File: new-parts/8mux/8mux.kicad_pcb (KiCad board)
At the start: 2 copper layers, 68.6 x 73.7 mm, 9 parts, among them J1 BHR-10-VUA, J2 BHR-10-VUA, J3 BHR-10-VUA, J4 Conn_01x01, K1 J104D2C12VDC.15S, K2 J104D2C12VDC.15S, K3 J104D2C12VDC.15S, K4 J104D2C12VDC.15S

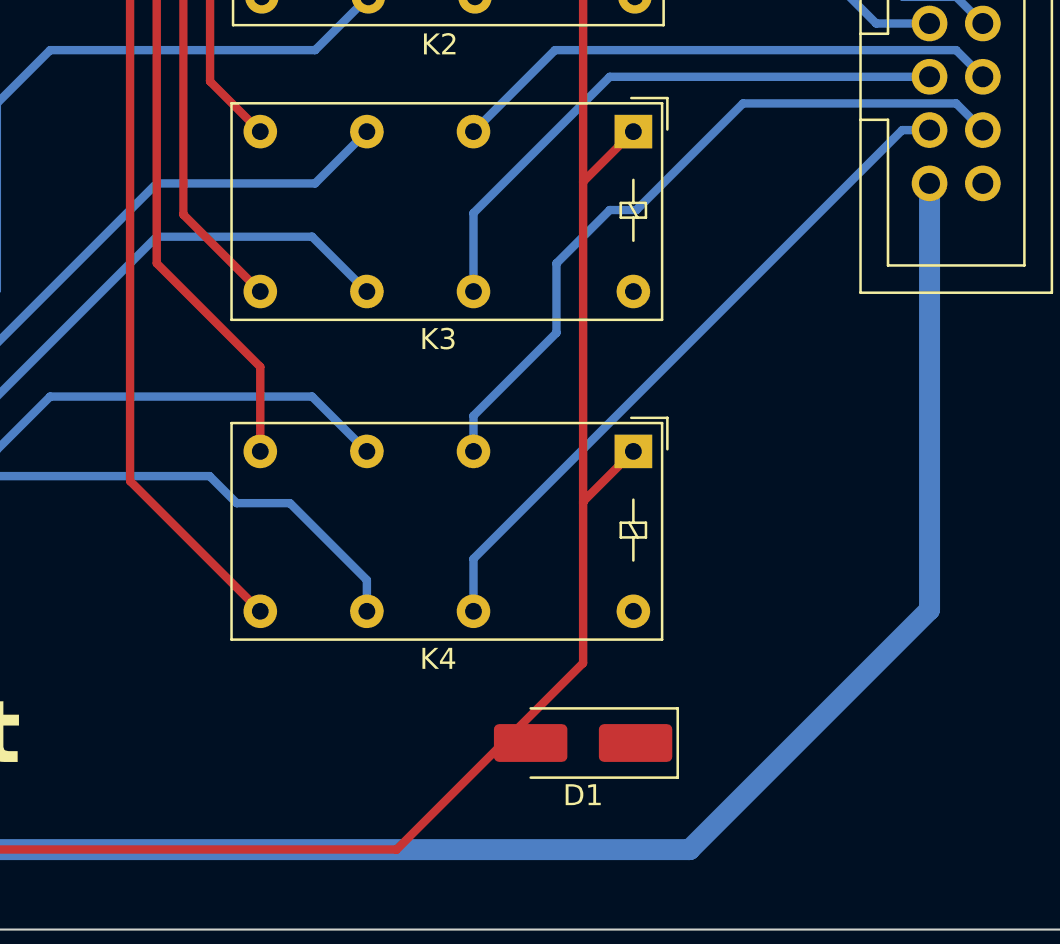
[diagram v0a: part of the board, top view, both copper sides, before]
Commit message: 8mux: Even out relay placement.
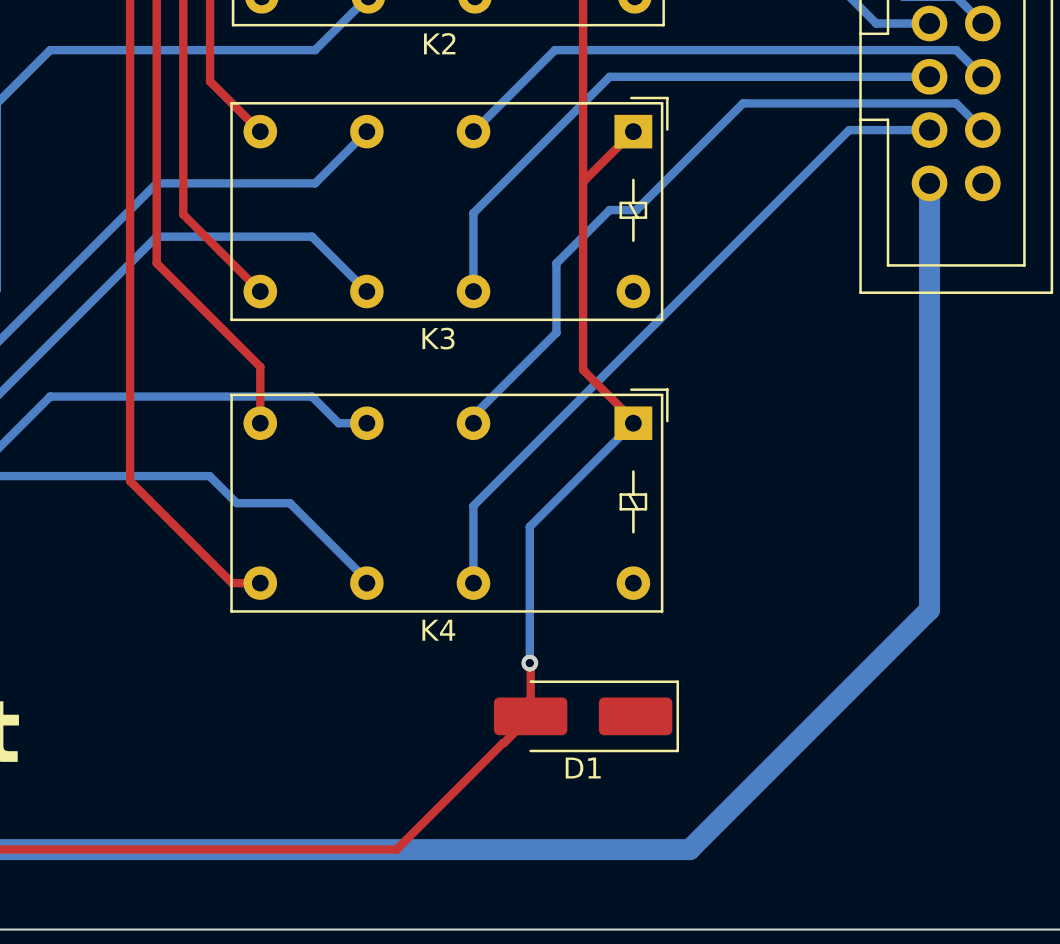
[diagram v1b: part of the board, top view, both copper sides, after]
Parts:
- moved K4 1.34 mm to (151.0, 113.0)
- moved D1 1.27 mm to (148.6, 127.0)
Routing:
- net Net-(D1-A2): track 106.5 -> 103.8 mm, vias 0 -> 1
- net Net-(J3-Pin_8): track 34.6 -> 33.3 mm
- net Net-(J2-Pin_7): track 30.6 -> 29.2 mm
- net Net-(J1-Pin_8): track 45.1 -> 43.7 mm
- net Net-(J2-Pin_8): track 26.1 -> 25.6 mm
- net Net-(J1-Pin_7): track 53.8 -> 53.2 mm
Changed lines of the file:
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@@
   )
   (footprint "Diode_SMD:D_SMA_Handsoldering" (layer "F.Cu")
-    (at 148.59 128.27 180)
+    (at 148.59 127 180)
     (descr "Diode SMA (DO-214AC) Handsoldering")
     (tags "Diode SMA (DO-214AC) Handsoldering")
@@
   )
   (footprint "Relay_THT:Relay_DPDT_Finder_30.22" (layer "F.Cu")
-    (at 150.985 114.3725 180)
+    (at 150.985 113.03 180)
     (descr "Finder 32.21-x000 Relay, DPDT, https://gfinder.findernet.com/public/attachments/30/EN/S30EN.pdf")
     (tags "AXICOM IM-Series Relay SPDT")
@@
   (gr_text "out" (at 161.29 83.82) (layer "F.SilkS")
     (effects (font (size 3 3) (thickness 0.6) bold) (justify left bottom))
+  )
+  (dimension (type aligned) (layer "F.SilkS")
+    (pts (xy 105.41 140.97) (xy 173.99 140.97))
+    (height 2.54)
+    (gr_text "68.5800 mm" (at 139.7 142.36) (layer "F.SilkS")
+      (effects (font (size 1 1) (thickness 0.15)))
+    )
+    (format (prefix "") (suffix "") (units 3) (units_format 1) (precision 4))
+    (style (thickness 0.15) (arrow_length 1.27) (text_position_mode 0) (extension_height 0.58642) (extension_offset 0.5) keep_text_aligned)
+  )
+  (dimension (type aligned) (layer "F.SilkS")
+    (pts (xy 101.6 63.5) (xy 101.6 137.16))
+    (height 2.54)
+    (gr_text "73.6600 mm" (at 97.91 100.33 90) (layer "F.SilkS")
+      (effects (font (size 1 1) (thickness 0.15)))
+    )
+    (format (prefix "") (suffix "") (units 3) (units_format 1) (precision 4))
+    (style (thickness 0.15) (arrow_length 1.27) (text_position_mode 0) (extension_height 0.58642) (extension_offset 0.5) keep_text_aligned)
   )
   (segment (start 131.8425 77.45) (end 133.205 78.8125) (width 0.4) (layer "F.Cu") (net 1))
@@
   (segment (start 130.81 96.7375) (end 130.81 83.82) (width 0.4) (layer "F.Cu") (net 6))
   (segment (start 128.27 81.28) (end 114.3 81.28) (width 0.4) (layer "F.Cu") (net 6))
+  (segment (start 113.03 85.09) (end 111.76 83.82) (width 0.4) (layer "F.Cu") (net 7))
+  (segment (start 133.205 120.65) (end 131.8625 120.65) (width 0.4) (layer "F.Cu") (net 7))
   (segment (start 124.46 85.09) (end 113.03 85.09) (width 0.4) (layer "F.Cu") (net 7))
+  (segment (start 131.8625 120.65) (end 127 115.7875) (width 0.4) (layer "F.Cu") (net 7))
+  (segment (start 127 115.7875) (end 127 87.63) (width 0.4) (layer "F.Cu") (net 7))
   (segment (start 127 87.63) (end 124.46 85.09) (width 0.4) (layer "F.Cu") (net 7))
-  (segment (start 113.03 85.09) (end 111.76 83.82) (width 0.4) (layer "F.Cu") (net 7))
-  (segment (start 133.205 121.9925) (end 127 115.7875) (width 0.4) (layer "F.Cu") (net 7))
-  (segment (start 127 115.7875) (end 127 87.63) (width 0.4) (layer "F.Cu") (net 7))
-  (segment (start 133.205 114.3725) (end 133.205 110.345) (width 0.4) (layer "F.Cu") (net 8))
+  (segment (start 128.27 86.36) (end 125.73 83.82) (width 0.4) (layer "F.Cu") (net 8))
   (segment (start 133.205 110.345) (end 128.27 105.41) (width 0.4) (layer "F.Cu") (net 8))
-  (segment (start 128.27 86.36) (end 125.73 83.82) (width 0.4) (layer "F.Cu") (net 8))
   (segment (start 125.73 83.82) (end 114.3 83.82) (width 0.4) (layer "F.Cu") (net 8))
+  (segment (start 133.205 113.03) (end 133.205 110.345) (width 0.4) (layer "F.Cu") (net 8))
   (segment (start 128.27 105.41) (end 128.27 86.36) (width 0.4) (layer "F.Cu") (net 8))
   (segment (start 138.285 78.8125) (end 135.8175 81.28) (width 0.4) (layer "B.Cu") (net 9))
@@
   (segment (start 111.76 129.54) (end 115.57 133.35) (width 1) (layer "B.Cu") (net 15))
   (segment (start 130.79 115.55) (end 113.01 115.55) (width 0.4) (layer "B.Cu") (net 17))
+  (segment (start 138.285 120.505) (end 134.62 116.84) (width 0.4) (layer "B.Cu") (net 17))
+  (segment (start 138.285 120.65) (end 138.285 120.505) (width 0.4) (layer "B.Cu") (net 17))
+  (segment (start 134.62 116.84) (end 132.08 116.84) (width 0.4) (layer "B.Cu") (net 17))
+  (segment (start 132.08 116.84) (end 130.79 115.55) (width 0.4) (layer "B.Cu") (net 17))
   (segment (start 113.01 115.55) (end 111.76 114.3) (width 0.4) (layer "B.Cu") (net 17))
-  (segment (start 138.285 121.9925) (end 138.285 120.505) (width 0.4) (layer "B.Cu") (net 17))
-  (segment (start 138.285 120.505) (end 134.62 116.84) (width 0.4) (layer "B.Cu") (net 17))
-  (segment (start 132.08 116.84) (end 130.79 115.55) (width 0.4) (layer "B.Cu") (net 17))
-  (segment (start 134.62 116.84) (end 132.08 116.84) (width 0.4) (layer "B.Cu") (net 17))
+  (segment (start 120.65 114.3) (end 114.3 114.3) (width 0.4) (layer "B.Cu") (net 18))
+  (segment (start 138.285 113.03) (end 136.9425 113.03) (width 0.4) (layer "B.Cu") (net 18))
+  (segment (start 123.19 111.76) (end 120.65 114.3) (width 0.4) (layer "B.Cu") (net 18))
+  (segment (start 136.9425 113.03) (end 135.6725 111.76) (width 0.4) (layer "B.Cu") (net 18))
   (segment (start 135.6725 111.76) (end 123.19 111.76) (width 0.4) (layer "B.Cu") (net 18))
-  (segment (start 138.285 114.3725) (end 135.6725 111.76) (width 0.4) (layer "B.Cu") (net 18))
-  (segment (start 123.19 111.76) (end 120.65 114.3) (width 0.4) (layer "B.Cu") (net 18))
-  (segment (start 120.65 114.3) (end 114.3 114.3) (width 0.4) (layer "B.Cu") (net 18))
   (segment (start 162.56 76.2) (end 165.1 78.74) (width 0.4) (layer "B.Cu") (net 19))
   (segment (start 165.1 78.74) (end 165.1 91.44) (width 0.4) (layer "B.Cu") (net 19))
@@
   (segment (start 143.365 99.1325) (end 147.2475 95.25) (width 0.4) (layer "B.Cu") (net 24))
   (segment (start 166.37 95.25) (end 167.64 96.52) (width 0.4) (layer "B.Cu") (net 24))
-  (segment (start 143.365 121.9925) (end 143.365 119.4925) (width 0.4) (layer "B.Cu") (net 25))
-  (segment (start 163.7975 99.06) (end 165.1 99.06) (width 0.4) (layer "B.Cu") (net 25))
-  (segment (start 143.365 119.4925) (end 163.7975 99.06) (width 0.4) (layer "B.Cu") (net 25))
+  (segment (start 143.365 120.65) (end 143.365 116.96875) (width 0.4) (layer "B.Cu") (net 25))
+  (segment (start 143.365 116.96875) (end 161.27375 99.06) (width 0.4) (layer "B.Cu") (net 25))
+  (segment (start 161.27375 99.06) (end 165.1 99.06) (width 0.4) (layer "B.Cu") (net 25))
+  (segment (start 146.09 124.5) (end 146.05 124.46) (width 0.4) (layer "F.Cu") (net 26))
+  (segment (start 148.59 110.49) (end 150.985 112.885) (width 0.4) (layer "F.Cu") (net 26))
   (segment (start 151.0575 85.09) (end 151.0575 85.1625) (width 0.4) (layer "F.Cu") (net 26))
   (segment (start 150.985 99.1325) (end 148.59 101.5275) (width 0.4) (layer "F.Cu") (net 26))
-  (segment (start 148.59 116.7675) (end 150.985 114.3725) (width 0.4) (layer "F.Cu") (net 26))
+  (segment (start 148.59 101.5275) (end 148.59 110.49) (width 0.4) (layer "F.Cu") (net 26))
   (segment (start 148.59 87.63) (end 148.59 101.5275) (width 0.4) (layer "F.Cu") (net 26))
-  (segment (start 148.59 116.84) (end 148.59 116.7675) (width 0.4) (layer "F.Cu") (net 26))
-  (segment (start 146.09 128.27) (end 144.78 128.27) (width 0.4) (layer "F.Cu") (net 26))
-  (segment (start 148.59 101.5275) (end 148.59 116.84) (width 0.4) (layer "F.Cu") (net 26))
+  (segment (start 150.985 112.885) (end 150.985 113.03) (width 0.4) (layer "F.Cu") (net 26))
   (segment (start 150.985 71.1925) (end 148.59 73.5875) (width 0.4) (layer "F.Cu") (net 26))
   (segment (start 151.0575 85.1625) (end 148.59 87.63) (width 0.4) (layer "F.Cu") (net 26))
+  (segment (start 146.09 127) (end 146.09 124.5) (width 0.4) (layer "F.Cu") (net 26))
+  (segment (start 146.09 127) (end 144.82 128.27) (width 0.4) (layer "F.Cu") (net 26))
   (segment (start 148.59 73.5875) (end 148.59 87.63) (width 0.4) (layer "F.Cu") (net 26))
-  (segment (start 148.59 124.46) (end 148.59 116.84) (width 0.4) (layer "F.Cu") (net 26))
-  (segment (start 144.78 128.27) (end 148.59 124.46) (width 0.4) (layer "F.Cu") (net 26))
   (segment (start 139.7 133.35) (end 144.78 128.27) (width 0.4) (layer "F.Cu") (net 26))
+  (segment (start 144.82 128.27) (end 144.78 128.27) (width 0.4) (layer "F.Cu") (net 26))
   (segment (start 111.76 133.35) (end 139.7 133.35) (width 0.4) (layer "F.Cu") (net 26))
+  (via (at 146.05 124.46) (size 0.8) (drill 0.4) (layers "F.Cu" "B.Cu") (net 26))
+  (segment (start 146.05 117.965) (end 150.985 113.03) (width 0.4) (layer "B.Cu") (net 26))
+  (segment (start 146.05 124.46) (end 146.05 117.965) (width 0.4) (layer "B.Cu") (net 26))
+  (segment (start 156.21 97.79) (end 166.37 97.79) (width 0.4) (layer "B.Cu") (net 27))
+  (segment (start 166.37 97.79) (end 167.64 99.06) (width 0.4) (layer "B.Cu") (net 27))
   (segment (start 147.32 105.41) (end 149.86 102.87) (width 0.4) (layer "B.Cu") (net 27))
   (segment (start 151.13 102.87) (end 156.21 97.79) (width 0.4) (layer "B.Cu") (net 27))
-  (segment (start 156.21 97.79) (end 166.37 97.79) (width 0.4) (layer "B.Cu") (net 27))
-  (segment (start 143.365 114.3725) (end 143.365 112.675443) (width 0.4) (layer "B.Cu") (net 27))
-  (segment (start 166.37 97.79) (end 167.64 99.06) (width 0.4) (layer "B.Cu") (net 27))
+  (segment (start 143.365 113.03) (end 143.365 112.675443) (width 0.4) (layer "B.Cu") (net 27))
+  (segment (start 147.32 108.720443) (end 147.32 105.41) (width 0.4) (layer "B.Cu") (net 27))
+  (segment (start 143.365 112.675443) (end 147.32 108.720443) (width 0.4) (layer "B.Cu") (net 27))
   (segment (start 149.86 102.87) (end 151.13 102.87) (width 0.4) (layer "B.Cu") (net 27))
-  (segment (start 143.365 112.675443) (end 147.32 108.720443) (width 0.4) (layer "B.Cu") (net 27))
-  (segment (start 147.32 108.720443) (end 147.32 105.41) (width 0.4) (layer "B.Cu") (net 27))
   (zone (net 16) (net_name "GND") (layer "F.Cu") (hatch edge 0.5)
     (connect_pads (clearance 0.5))
